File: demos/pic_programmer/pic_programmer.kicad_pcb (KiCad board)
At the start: 2 copper layers, 68 parts, among them J1 DB9-FEMAL, P1 CONN_2, P2 SUPP28, P3 SUPP40, Q1 BC237, Q2 BC307, Q3 BC307, U1 24Cxx, U2 74HC125, U3 7805, U4 LT1373, U5 PIC_18_PINS, U6 PIC_8_PINS

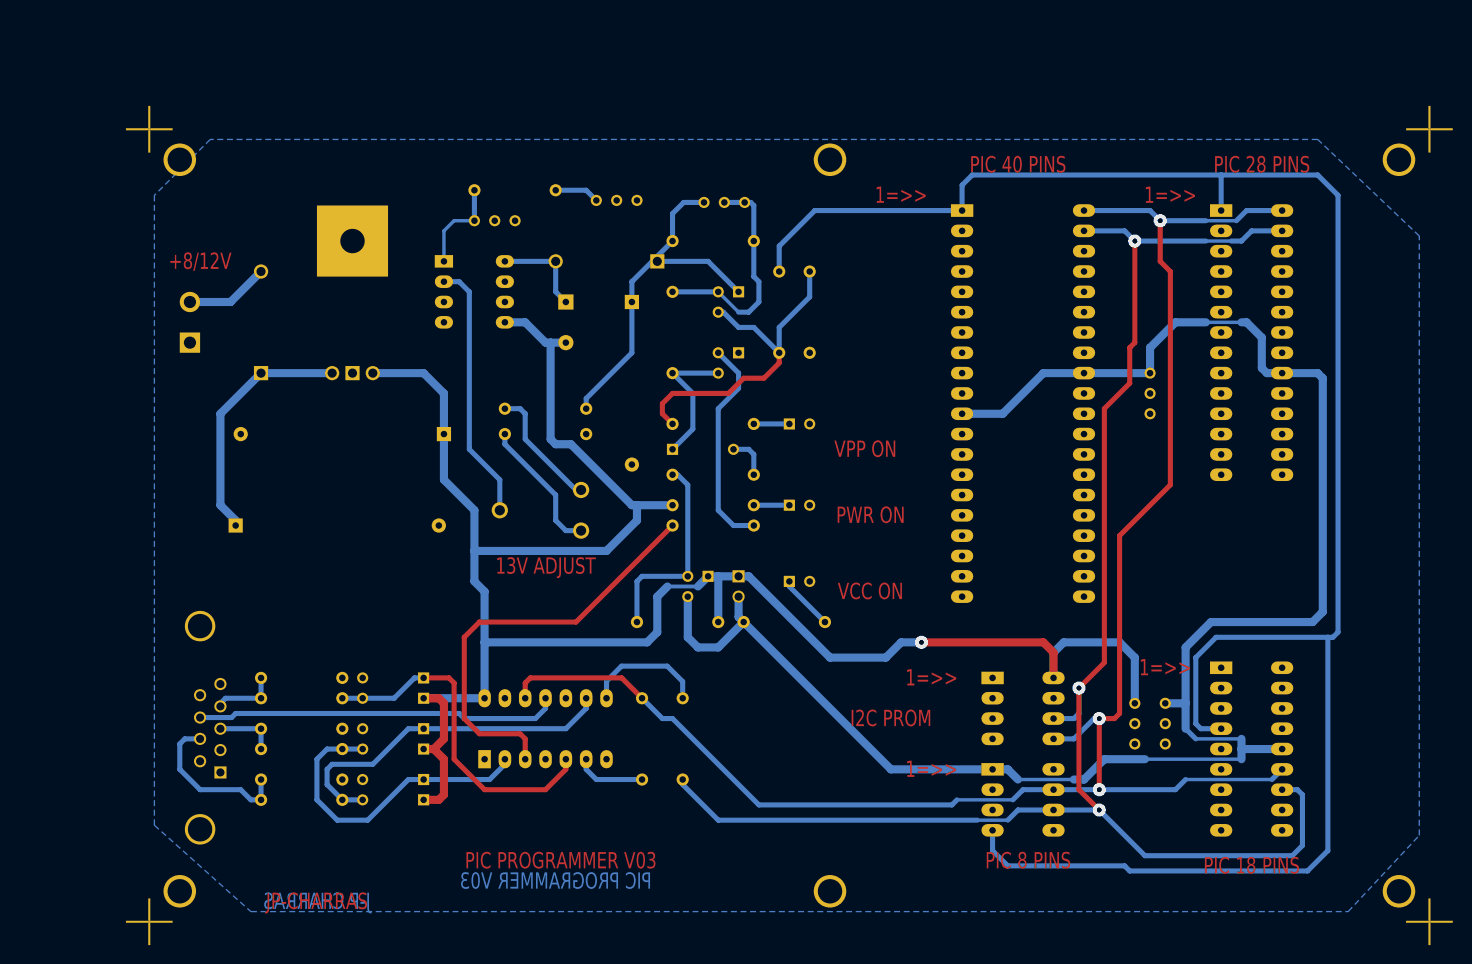
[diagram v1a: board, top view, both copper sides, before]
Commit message: Update demos. Fix  pspice netlist issues when using ( and ) in net names ( parenthesis are replaced by underscore) .
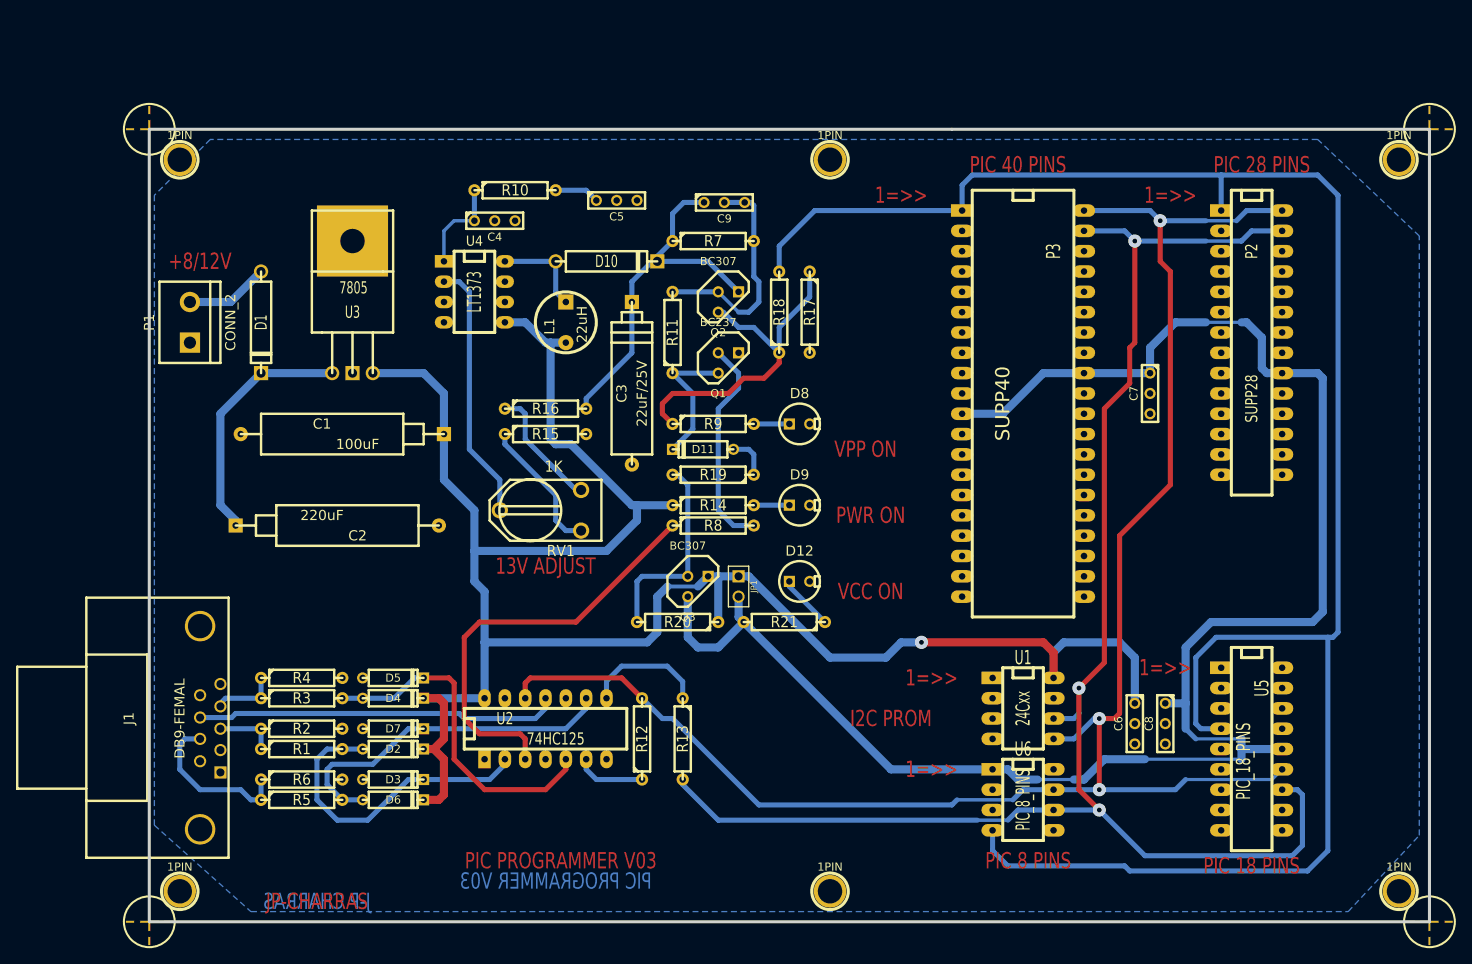
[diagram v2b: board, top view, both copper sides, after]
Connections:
- net /PC-DATA-IN renamed /CTS
- net /VPP/MCLR renamed /pic_sockets.sch/VPP-MCLR
- net /VPP_ON renamed /TXD
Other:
- board outline added: 160 x 99.1 mm
- net class Default: clearance 0.254 -> 0.25; trace_width 0.254 -> 0.6; via_dia 0.889 -> 1.6; via_drill 0.635 -> 0.6
- net class POWER added: clearance 0.28, trace_width 1, via_dia 1.6, via_drill 0.6
- rule pad_to_mask_clearance: 0.2 -> 0.1
- rule trace_clearance: 0.254 -> 0.25

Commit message: Pcbnew: Minor fix in hotkeys. Demos: add an example to use  a local fp-lib-table and local libs, and update schematics and boards.
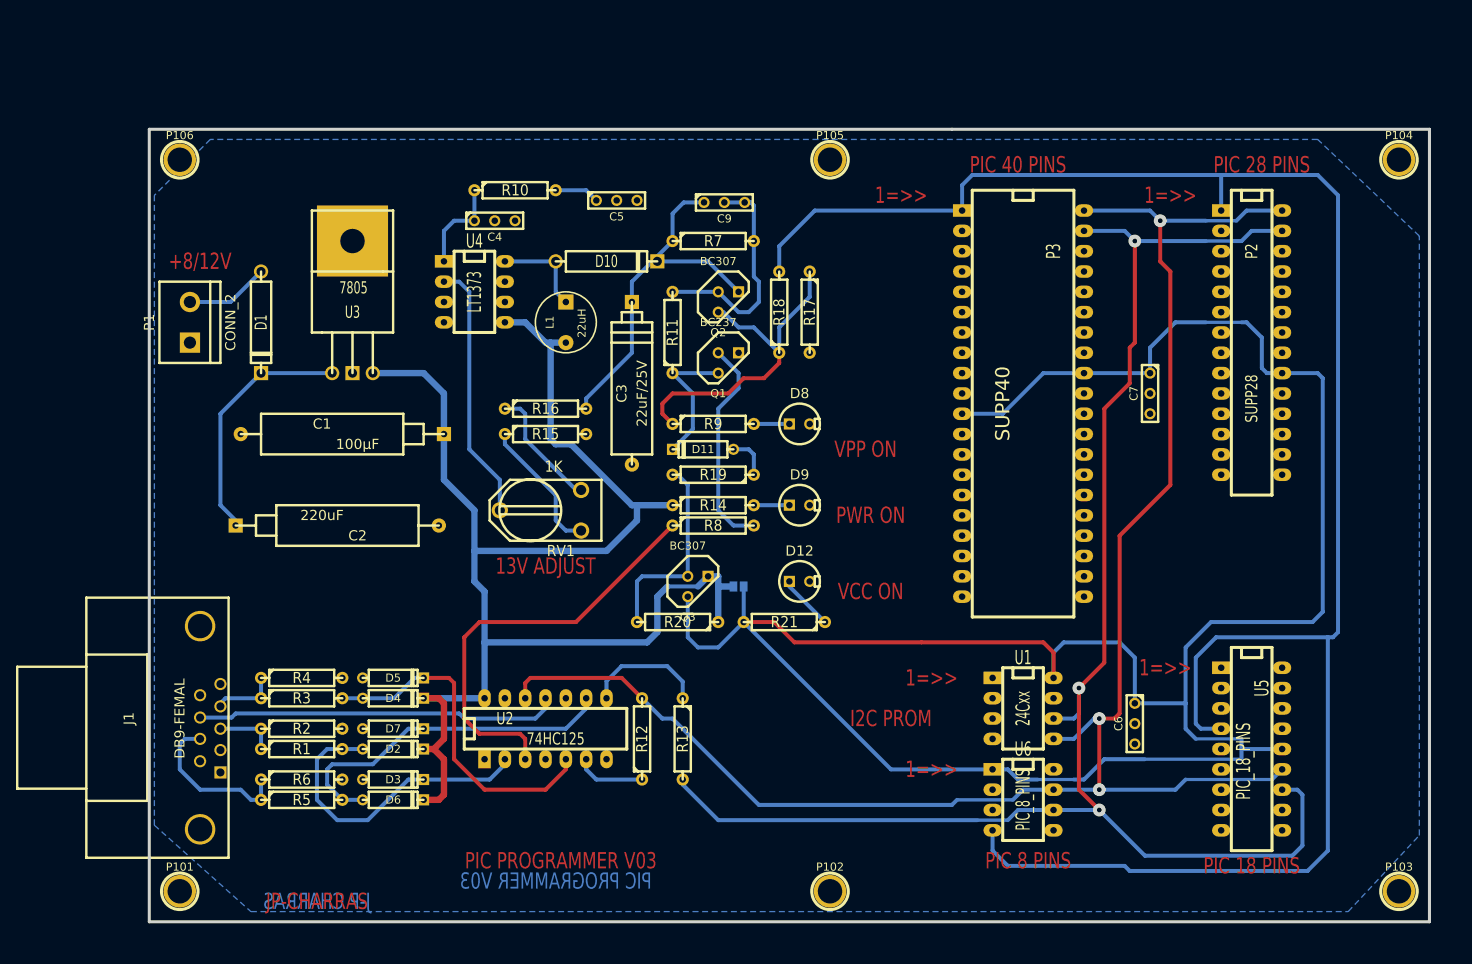
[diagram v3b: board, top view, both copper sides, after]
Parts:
- removed 1PIN (x6): P***, 1pin
- removed C8: 100nF, C1-1
- removed MIRE (x4): *, MIRE
- added P101: CONN_1, footprints:1pin-4, F.Cu at (77.5, 135.9)
- added P102: CONN_1, footprints:1pin-4, F.Cu at (158.8, 135.9)
- added P103: CONN_1, footprints:1pin-4, F.Cu at (229.9, 135.9)
- added P104: CONN_1, footprints:1pin-4, F.Cu at (229.9, 44.5)
- added P105: CONN_1, footprints:1pin-4, F.Cu at (158.8, 44.5)
- added P106: CONN_1, footprints:1pin-4, F.Cu at (77.5, 44.5)
- C1: value 100uF -> 100µF; footprint CP10 -> discret:CP10
- C2: footprint CP10 -> discret:CP10
- C3: footprint CP8 -> discret:CP8
- C4, C5, C6, C7, C9: footprint C1-1 -> discret:C1-1
- D1, D10: footprint D5 -> discret:D5
- D11, D2, D3, D4, D5, D6, D7: footprint D3 -> discret:D3
- D12, D8, D9: footprint LEDV -> discret:LEDV
- J1: footprint DB9FC -> connect:DB9FC
- JP1: footprint PIN_ARRAY_2X1 -> connect:GS2; moved to B.Cu
- L1: footprint INDUCTOR_V -> inductors:INDUCTOR_V
- P1: footprint bornier2 -> connect:bornier2
- P2: footprint 28DIP-ELL300 -> dip_sockets:DIP-28__300_ELL
- P3: footprint 40DIP-ELL600 -> footprints:textool_40
- Q1, Q2, Q3: footprint TO92 -> discret:TO92
- R1, R10, R11, R12, R13, R14, R15, R16, R17, R18, R19, R2, R20, R21, R3, R4, R5, R6, R7, R8, R9: footprint R4 -> discret:R4
- RV1: footprint RV2X4 -> discret:RV2X4
- U1, U4, U6: footprint 8DIP-ELL300 -> dip_sockets:DIP-8__300_ELL
- U2: footprint 14DIP-ELL300 -> dip_sockets:DIP-14__300_ELL
- U3: footprint LM78XX -> discret:LM78XX
- U5: footprint 18DIP-ELL300 -> dip_sockets:DIP-18__300_ELL
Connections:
- net /pic_sockets.sch/CLOCK-RB6 renamed /pic_sockets/CLOCK-RB6
- net /pic_sockets.sch/DATA-RB7 renamed /pic_sockets/DATA-RB7
- net /pic_sockets.sch/VPP-MCLR renamed /pic_sockets/VPP-MCLR
- C6 pad 1: VCC -> /pic_sockets/VCC_PIC
- C7 pad 1: /pic_sockets.sch/VCC_PIC -> /pic_sockets/VCC_PIC
- JP1 pad 2: /pic_sockets.sch/VCC_PIC -> /pic_sockets/VCC_PIC
- P2 pad 20: /pic_sockets.sch/VCC_PIC -> /pic_sockets/VCC_PIC
- P3 pad 11: /pic_sockets.sch/VCC_PIC -> /pic_sockets/VCC_PIC
- P3 pad 32: /pic_sockets.sch/VCC_PIC -> /pic_sockets/VCC_PIC
- Q3 pad 3: /pic_sockets.sch/VCC_PIC -> /pic_sockets/VCC_PIC
- R21 pad 2: /pic_sockets.sch/VCC_PIC -> /pic_sockets/VCC_PIC
- U1 pad 8: VCC -> /pic_sockets/VCC_PIC
- U5 pad 14: /pic_sockets.sch/VCC_PIC -> /pic_sockets/VCC_PIC
- U6 pad 1: /pic_sockets.sch/VCC_PIC -> /pic_sockets/VCC_PIC
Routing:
- net /pic_sockets/VCC_PIC: track 0.00 -> 290.3 mm
- net /pic_sockets.sch/VCC_PIC: track 221.6 -> 0.00 mm
- net VCC: track 252.2 -> 183.3 mm, vias 1 -> 0
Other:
- net class Default: trace_width 0.6 -> 0.5
- net class POWER: trace_width 1 -> 0.8

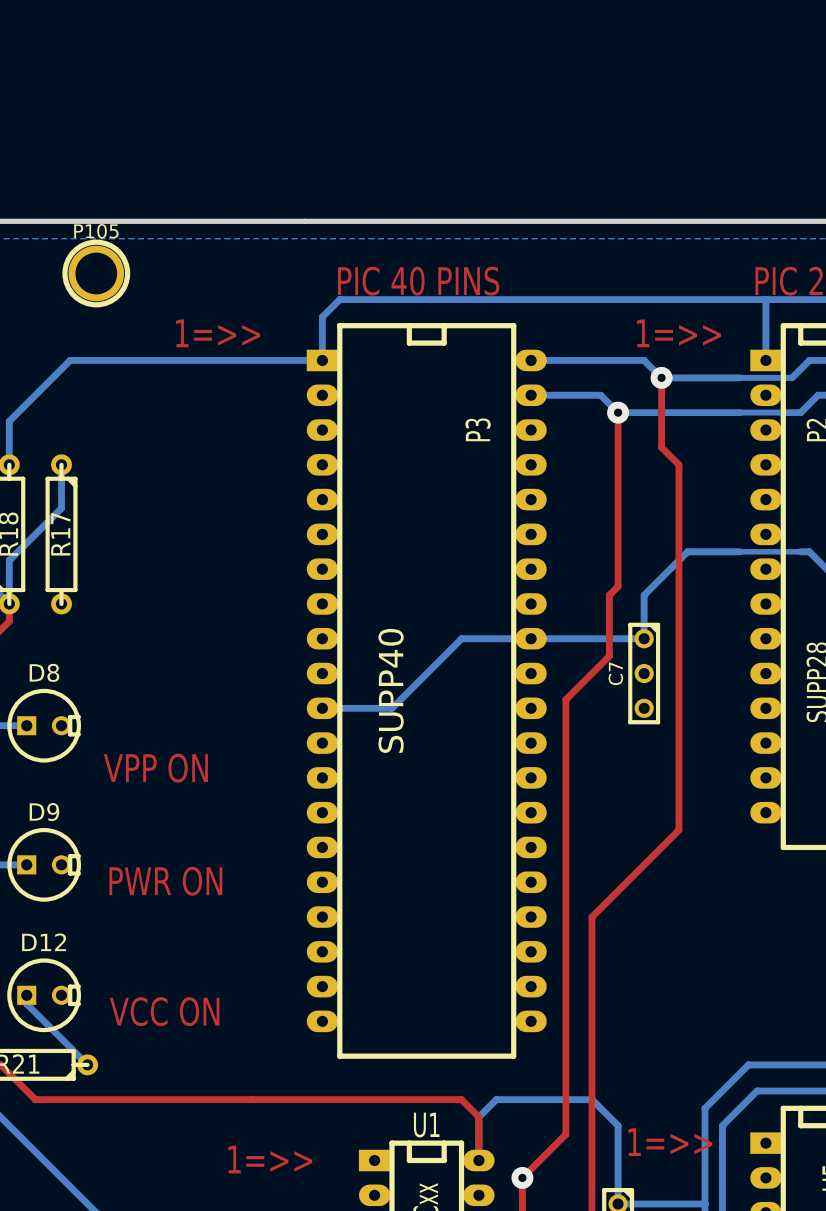
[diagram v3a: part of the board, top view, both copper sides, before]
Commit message: Minor fixes: specctra export: skip malformed circles (having a radius = 0)  in board outline creation, which can crash 3d-viewer or vrml export. dialog_fp_lib_table: remember during a session the last open table (global or local). drawing_tool: fix compil warning Update demos.
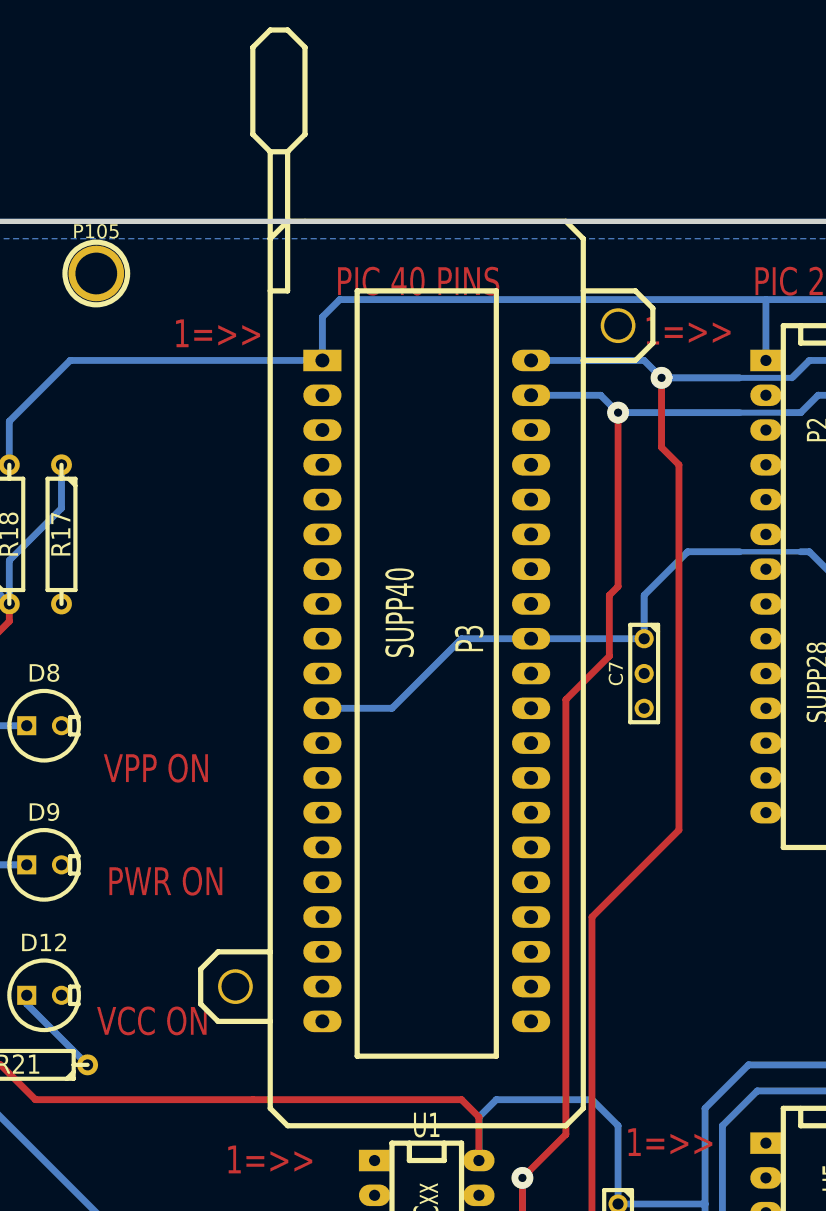
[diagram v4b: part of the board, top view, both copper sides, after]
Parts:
- P3: footprint footprints:textool_40 -> sockets:40tex-Ell600

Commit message: merge from production bzr6934 to bzr 6953
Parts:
- C1, C2: footprint discret:CP10 -> Discret:CP10
- C3: footprint discret:CP8 -> Discret:CP8
- C4, C5, C6, C7: footprint discret:C1-1 -> Discret:C1-1
- C9: value 22OnF -> 220nF; footprint discret:C1-1 -> Discret:C1-1
- D1, D10: footprint discret:D5 -> Discret:D5
- D11, D2, D3, D4, D5, D6, D7: footprint discret:D3 -> Discret:D3
- D12, D8, D9: footprint discret:LEDV -> Discret:LEDV
- Q1, Q2, Q3: footprint discret:TO92 -> Discret:TO92
- R1, R10, R11, R12, R13, R14, R15, R16, R17, R18, R19, R2, R20, R21, R3, R4, R5, R6, R7, R8, R9: footprint discret:R4 -> Discret:R4
- RV1: footprint discret:RV2X4 -> Discret:RV2X4
- U3: footprint discret:LM78XX -> Discret:LM78XX
- turned D12 to 180 degrees
- turned D8 to 180 degrees
- turned D9 to 180 degrees
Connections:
- net /pic_sockets/CLOCK-RB6 renamed /CLOCK-RB6
- net /pic_sockets/DATA-RB7 renamed /DATA-RB7
- net /pic_sockets/VPP-MCLR renamed /VPP/MCLR
- D1 pad 1: Net-(D1-Pad1) -> Net-(C2-Pad1)
- D1 pad 2: Net-(C2-Pad1) -> Net-(D1-Pad2)
- D10 pad 1: Net-(D10-Pad1) -> VPP
- D10 pad 2: VPP -> Net-(D10-Pad2)
- D12 pad 1: Net-(D12-Pad1) -> GND
- D12 pad 2: GND -> Net-(D12-Pad2)
- D2 pad 1: Net-(D2-Pad1) -> VCC
- D2 pad 2: VCC -> Net-(D2-Pad2)
- D3 pad 1: GND -> Net-(D2-Pad2)
- D3 pad 2: Net-(D2-Pad1) -> GND
- D4 pad 1: Net-(D4-Pad1) -> VCC
- D4 pad 2: VCC -> Net-(D4-Pad2)
- D5 pad 1: GND -> Net-(D4-Pad2)
- D5 pad 2: Net-(D4-Pad1) -> GND
- D6 pad 1: Net-(D6-Pad1) -> VCC
- D6 pad 2: VCC -> Net-(D6-Pad2)
- D7 pad 1: GND -> Net-(D6-Pad2)
- D7 pad 2: Net-(D6-Pad1) -> GND
- D8 pad 1: Net-(D8-Pad1) -> GND
- D8 pad 2: GND -> Net-(D8-Pad2)
- D9 pad 1: Net-(D9-Pad1) -> GND
- D9 pad 2: GND -> Net-(D9-Pad2)
- J1 pad 1: (no net) -> Net-(J1-Pad1)
- J1 pad 2: (no net) -> Net-(J1-Pad2)
- J1 pad 6: (no net) -> Net-(J1-Pad6)
- J1 pad 9: (no net) -> Net-(J1-Pad9)
- L1 pad 1: Net-(D10-Pad1) -> Net-(D10-Pad2)
- P1 pad 2: Net-(D1-Pad1) -> Net-(D1-Pad2)
- P101 pad 1: (no net) -> Net-(P101-Pad1)
- P102 pad 1: (no net) -> Net-(P102-Pad1)
- P103 pad 1: (no net) -> Net-(P103-Pad1)
- P104 pad 1: (no net) -> Net-(P104-Pad1)
- P105 pad 1: (no net) -> Net-(P105-Pad1)
- P106 pad 1: (no net) -> Net-(P106-Pad1)
- P2 pad 10: (no net) -> Net-(P2-Pad10)
- P2 pad 11: (no net) -> Net-(P2-Pad11)
- P2 pad 12: (no net) -> Net-(P2-Pad12)
- P2 pad 13: (no net) -> Net-(P2-Pad13)
- P2 pad 14: (no net) -> Net-(P2-Pad14)
- P2 pad 15: (no net) -> Net-(P2-Pad15)
- P2 pad 16: (no net) -> Net-(P2-Pad16)
- P2 pad 17: (no net) -> Net-(P2-Pad17)
- P2 pad 18: (no net) -> Net-(P2-Pad18)
- P2 pad 2: (no net) -> Net-(P2-Pad2)
- P2 pad 21: (no net) -> Net-(P2-Pad21)
- P2 pad 22: (no net) -> Net-(P2-Pad22)
- P2 pad 23: (no net) -> Net-(P2-Pad23)
- P2 pad 24: (no net) -> Net-(P2-Pad24)
- P2 pad 25: (no net) -> Net-(P2-Pad25)
- P2 pad 26: (no net) -> Net-(P2-Pad26)
- P2 pad 3: (no net) -> Net-(P2-Pad3)
- P2 pad 4: (no net) -> Net-(P2-Pad4)
- P2 pad 5: (no net) -> Net-(P2-Pad5)
- P2 pad 6: (no net) -> Net-(P2-Pad6)
- P2 pad 7: (no net) -> Net-(P2-Pad7)
- P2 pad 9: (no net) -> Net-(P2-Pad9)
- P3 pad 10: (no net) -> Net-(P3-Pad10)
- P3 pad 13: (no net) -> Net-(P3-Pad13)
- P3 pad 14: (no net) -> Net-(P3-Pad14)
- P3 pad 15: (no net) -> Net-(P3-Pad15)
- P3 pad 16: (no net) -> Net-(P3-Pad16)
- P3 pad 17: (no net) -> Net-(P3-Pad17)
- P3 pad 18: (no net) -> Net-(P3-Pad18)
- P3 pad 19: (no net) -> Net-(P3-Pad19)
- P3 pad 2: (no net) -> Net-(P3-Pad2)
- P3 pad 20: (no net) -> Net-(P3-Pad20)
- P3 pad 21: (no net) -> Net-(P3-Pad21)
- P3 pad 22: (no net) -> Net-(P3-Pad22)
- P3 pad 23: (no net) -> Net-(P3-Pad23)
- P3 pad 24: (no net) -> Net-(P3-Pad24)
- P3 pad 25: (no net) -> Net-(P3-Pad25)
- P3 pad 26: (no net) -> Net-(P3-Pad26)
- P3 pad 27: (no net) -> Net-(P3-Pad27)
- P3 pad 28: (no net) -> Net-(P3-Pad28)
- P3 pad 29: (no net) -> Net-(P3-Pad29)
- P3 pad 3: (no net) -> Net-(P3-Pad3)
- P3 pad 30: (no net) -> Net-(P3-Pad30)
- P3 pad 33: (no net) -> Net-(P3-Pad33)
- P3 pad 34: (no net) -> Net-(P3-Pad34)
- P3 pad 35: (no net) -> Net-(P3-Pad35)
- P3 pad 36: (no net) -> Net-(P3-Pad36)
- P3 pad 37: (no net) -> Net-(P3-Pad37)
- P3 pad 38: (no net) -> Net-(P3-Pad38)
- P3 pad 4: (no net) -> Net-(P3-Pad4)
- P3 pad 5: (no net) -> Net-(P3-Pad5)
- P3 pad 6: (no net) -> Net-(P3-Pad6)
- P3 pad 7: (no net) -> Net-(P3-Pad7)
- P3 pad 9: (no net) -> Net-(P3-Pad9)
- Q1 pad 3: Net-(D11-Pad2) -> Net-(D11-Pad1)
- R1 pad 2: Net-(D2-Pad1) -> Net-(D2-Pad2)
- R11 pad 1: Net-(D11-Pad2) -> Net-(D11-Pad1)
- R14 pad 2: Net-(D9-Pad1) -> Net-(D9-Pad2)
- R19 pad 1: Net-(D11-Pad1) -> Net-(D11-Pad2)
- R21 pad 1: Net-(D12-Pad1) -> Net-(D12-Pad2)
- R3 pad 2: Net-(D4-Pad1) -> Net-(D4-Pad2)
- R5 pad 2: Net-(D6-Pad1) -> Net-(D6-Pad2)
- R9 pad 2: Net-(D8-Pad1) -> Net-(D8-Pad2)
- U1 pad 7: (no net) -> Net-(U1-Pad7)
- U2 pad 2: Net-(D2-Pad1) -> Net-(D2-Pad2)
- U2 pad 5: Net-(D4-Pad1) -> Net-(D4-Pad2)
- U2 pad 9: Net-(D6-Pad1) -> Net-(D6-Pad2)
- U4 pad 3: (no net) -> Net-(U4-Pad3)
- U4 pad 4: (no net) -> Net-(U4-Pad4)
- U4 pad 8: Net-(D10-Pad1) -> Net-(D10-Pad2)
- U5 pad 1: (no net) -> Net-(U5-Pad1)
- U5 pad 10: (no net) -> Net-(U5-Pad10)
- U5 pad 11: (no net) -> Net-(U5-Pad11)
- U5 pad 15: (no net) -> Net-(U5-Pad15)
- U5 pad 16: (no net) -> Net-(U5-Pad16)
- U5 pad 17: (no net) -> Net-(U5-Pad17)
- U5 pad 18: (no net) -> Net-(U5-Pad18)
- U5 pad 2: (no net) -> Net-(U5-Pad2)
- U5 pad 3: (no net) -> Net-(U5-Pad3)
- U5 pad 6: (no net) -> Net-(U5-Pad6)
- U5 pad 7: (no net) -> Net-(U5-Pad7)
- U5 pad 8: (no net) -> Net-(U5-Pad8)
- U5 pad 9: (no net) -> Net-(U5-Pad9)
- U6 pad 2: (no net) -> Net-(U6-Pad2)
- U6 pad 3: (no net) -> Net-(U6-Pad3)
- U6 pad 5: (no net) -> Net-(U6-Pad5)
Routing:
- net Net-(D6-Pad2): track 0.00 -> 44.0 mm
- net Net-(D6-Pad1): track 44.0 -> 0.00 mm
- net Net-(D4-Pad1): track 42.7 -> 0.00 mm
- net Net-(D4-Pad2): track 0.00 -> 42.7 mm
- net Net-(D2-Pad2): track 0.00 -> 39.4 mm
- net Net-(D2-Pad1): track 39.4 -> 0.00 mm
- net Net-(D11-Pad2): track 17.3 -> 5.34 mm
- net Net-(D11-Pad1): track 5.34 -> 17.3 mm
- net Net-(D10-Pad2): track 0.00 -> 12.0 mm
- net Net-(D10-Pad1): track 12.0 -> 0.00 mm
- net Net-(D1-Pad2): track 0.00 -> 10.5 mm
- net Net-(D1-Pad1): track 10.5 -> 0.00 mm
- net Net-(D12-Pad2): track 0.00 -> 6.92 mm
- net Net-(D12-Pad1): track 6.92 -> 0.00 mm
- net Net-(D9-Pad2): track 0.00 -> 4.44 mm
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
